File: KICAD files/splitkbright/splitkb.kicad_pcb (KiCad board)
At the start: 2 copper layers, 131.3 x 114.6 mm, 83 parts, among them SW31 SW_Push, SW32 SW_Push, SW37 SW_Push, SW38 SW_Push, SW39 SW_Push, SW40 SW_Push, SW41 SW_Push, SW42 SW_Push, SW43 SW_Push, SW44 SW_Push, SW45 SW_Push, SW46 SW_Push, SW47 SW_Push, SW48 SW_Push, SW49 SW_Push, SW50 SW_Push, SW51 SW_Push, SW52 SW_Push, SW53 SW_Push, SW54 SW_Push, SW55 SW_Push, SW56 SW_Push, SW57 SW_Push, SW58 SW_Push, SW59 SW_Push, SW60 SW_Push, SW61 SW_Push, SW62 SW_Push, SW63 SW_Push, SW64 SW_Push, SW65 SW_Push, SW66 SW_Push, SW67 SW_Push, SW68 SW_Push, SW69 SW_Push, SW70 SW_Push, SW71 SW_Push, SW72 SW_Push, SW73 SW_Push, SW74 SW_Push, U1 nice_nano

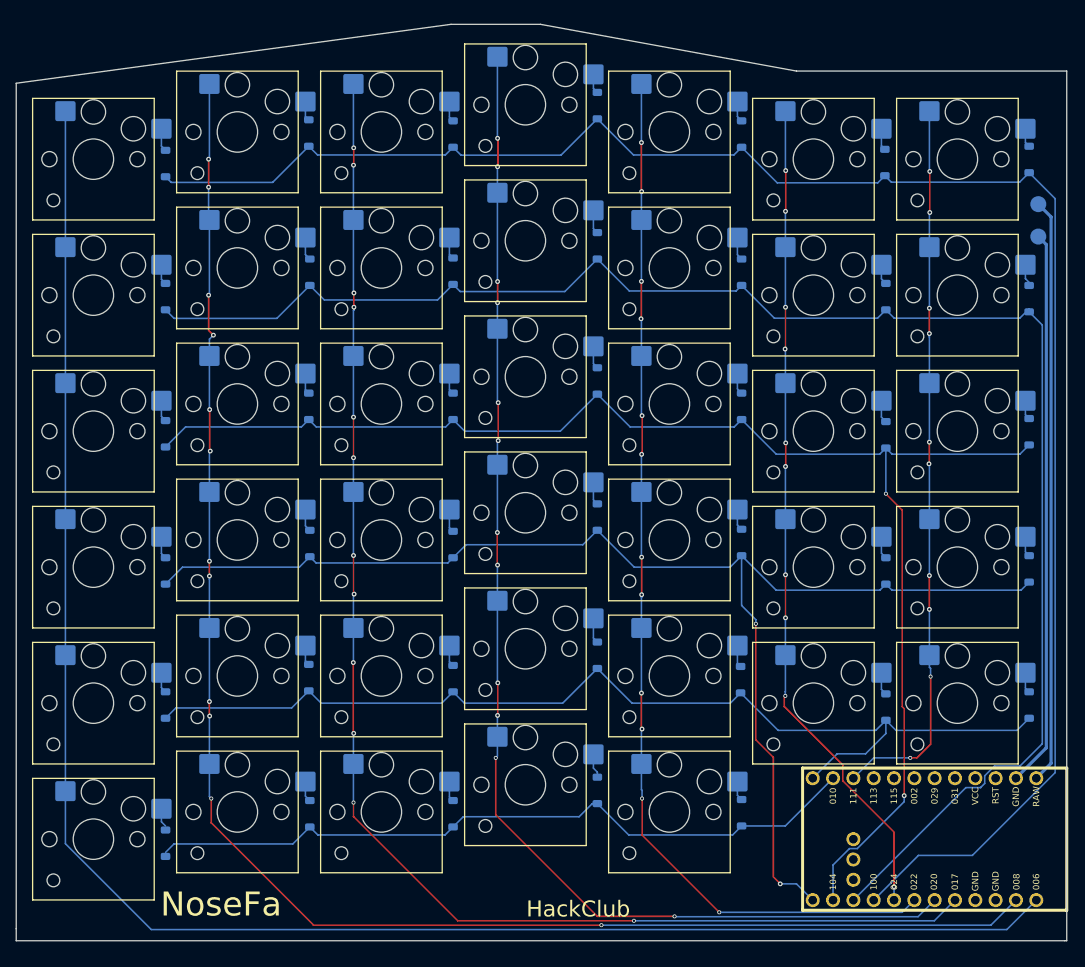
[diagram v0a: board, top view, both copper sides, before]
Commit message: Edited PCBs
- Added mounting holes to both pcbs and schematics
- Changed the shape and size of both PCBs
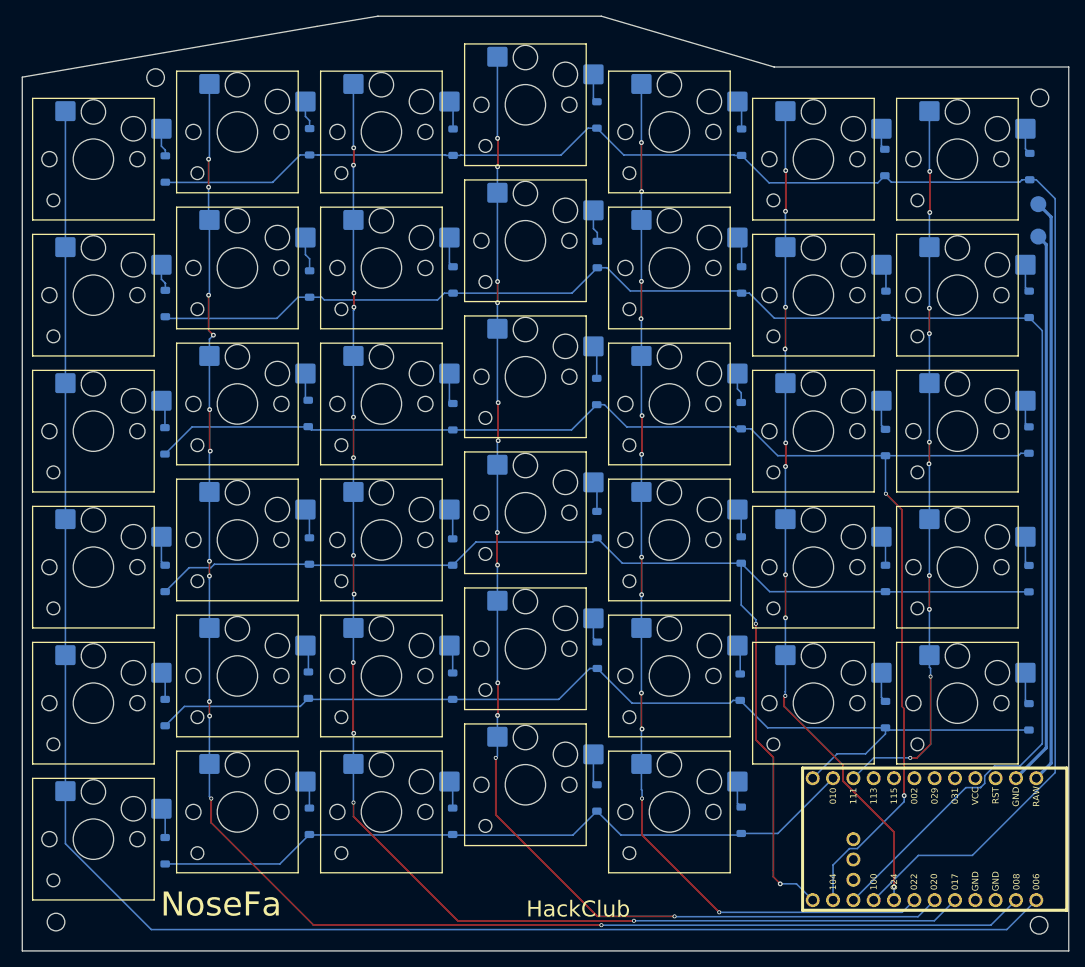
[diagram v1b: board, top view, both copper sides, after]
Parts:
- added REF**: MountingHole_2.2mm_M2, MountingHole:MountingHole_2.2mm_M2, F.Cu at (262.3, 43.3)
- added REF**: MountingHole_2.2mm_M2, MountingHole:MountingHole_2.2mm_M2, F.Cu at (139.3, 146.4)
- added REF**: MountingHole_2.2mm_M2, MountingHole:MountingHole_2.2mm_M2, F.Cu at (262.2, 146.8)
- added REF**: MountingHole_2.2mm_M2, MountingHole:MountingHole_2.2mm_M2, F.Cu at (151.8, 40.8)
- moved D58 1.47 mm to (171.0, 66.6)
- moved D73 1.47 mm to (260.9, 120.7)
- moved D47 1.32 mm to (206.9, 80.0)
- moved D53 1.30 mm to (188.9, 83.2)
- moved D72 1.22 mm to (260.9, 103.4)
- moved D42 1.17 mm to (225.0, 83.1)
- moved D45 1.17 mm to (206.9, 45.5)
- moved D57 1.10 mm to (171.0, 48.8)
- moved D46 1.09 mm to (207.0, 62.9)
- moved D52 1.09 mm to (189.0, 66.1)
- moved D71 1.04 mm to (260.9, 86.1)
- moved D40 1.02 mm to (225.0, 48.9)
- moved D51 1.02 mm to (189.0, 48.9)
- moved D37 0.97 mm to (243.0, 86.4)
- moved D32 0.97 mm to (243.1, 69.1)
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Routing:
- net row1: track 206.0 -> 199.9 mm
- net row4: track 132.0 -> 126.7 mm
- net row2: track 179.4 -> 174.4 mm
- net row0: track 224.2 -> 219.9 mm
- net row3: track 164.6 -> 160.7 mm
- net Net-(D73-A): track 2.58 -> 4.04 mm
- net Net-(D58-A): track 2.91 -> 4.37 mm
- net Net-(D68-A): track 2.36 -> 3.79 mm
- net Net-(D47-A): track 2.88 -> 4.17 mm
- net Net-(D53-A): track 2.64 -> 3.92 mm
- net Net-(D72-A): track 2.56 -> 3.77 mm
- net Net-(D45-A): track 2.46 -> 3.61 mm
- net Net-(D42-A): track 2.67 -> 3.81 mm
- net Net-(D57-A): track 2.46 -> 3.59 mm
- net Net-(D46-A): track 2.98 -> 4.08 mm
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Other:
- board size 131.3 x 114.6 mm -> 130.8 x 116.8 mm

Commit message: Edited PCB.
- Changed the footprint used for the dev board.
- Ran traces again for the dev board.
- Made a custom symbol and footprint for the devboard.
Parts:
- removed the REF** at (262.3, 43.3)
- removed the REF** at (139.3, 146.4)
- removed the REF** at (262.2, 146.8)
- removed the REF** at (151.8, 40.8)
- added D1: D, Diode_SMD:D_SOD-123, B.Cu at (52.8, 87.7)
- added D10: D, Diode_SMD:D_SOD-123, B.Cu at (106.9, 79.3)
- added D11: D, Diode_SMD:D_SOD-123, B.Cu at (124.8, 83.0)
- added D12: D, Diode_SMD:D_SOD-123, B.Cu at (52.8, 104.1)
- added D13: D, Diode_SMD:D_SOD-123, B.Cu at (71.0, 104.1)
- added D14: D, Diode_SMD:D_SOD-123, B.Cu at (88.9, 99.7)
- added D15: D, Diode_SMD:D_SOD-123, B.Cu at (106.9, 96.3)
- added D16: D, Diode_SMD:D_SOD-123, B.Cu at (124.9, 99.7)
- added D17: D, Diode_SMD:D_SOD-123, B.Cu at (52.9, 121.7)
- added D18: D, Diode_SMD:D_SOD-123, B.Cu at (70.7, 121.3)
- added D19: D, Diode_SMD:D_SOD-123, B.Cu at (88.9, 116.7)
- added D2: D, Diode_SMD:D_SOD-123, B.Cu at (52.8, 69.8)
- added D20: D, Diode_SMD:D_SOD-123, B.Cu at (106.9, 113.3)
- added D21: D, Diode_SMD:D_SOD-123, B.Cu at (124.9, 116.7)
- added D22: D, Diode_SMD:D_SOD-123, B.Cu at (52.8, 137.7)
- added D23: D, Diode_SMD:D_SOD-123, B.Cu at (70.9, 137.7)
- added D24: D, Diode_SMD:D_SOD-123, B.Cu at (88.9, 133.7)
- added D25: D, Diode_SMD:D_SOD-123, B.Cu at (106.9, 130.3)
- added D26: D, Diode_SMD:D_SOD-123, B.Cu at (124.8, 133.7)
- added D27: D, Diode_SMD:D_SOD-123, B.Cu at (142.8, 117.8)
- added D28: D, Diode_SMD:D_SOD-123, B.Cu at (142.9, 134.6)
- added D29: D, Diode_SMD:D_SOD-123, B.Cu at (142.9, 83.5)
- added D3: D, Diode_SMD:D_SOD-123, B.Cu at (70.8, 70.0)
- added D30: D, Diode_SMD:D_SOD-123, B.Cu at (142.9, 101.4)
- added D33: D, Diode_SMD:D_SOD-123, B.Cu at (88.9, 150.7)
- added D34: D, Diode_SMD:D_SOD-123, B.Cu at (106.9, 147.3)
- added D35: D, Diode_SMD:D_SOD-123, B.Cu at (124.9, 150.7)
- added D36: D, Diode_SMD:D_SOD-123, B.Cu at (142.9, 151.4)
- added D4: D, Diode_SMD:D_SOD-123, B.Cu at (88.9, 65.7)
- added D5: D, Diode_SMD:D_SOD-123, B.Cu at (106.9, 62.3)
- added D6: D, Diode_SMD:D_SOD-123, B.Cu at (124.9, 65.7)
- added D7: D, Diode_SMD:D_SOD-123, B.Cu at (143.0, 66.4)
- added D8: D, Diode_SMD:D_SOD-123, B.Cu at (70.7, 87.3)
- added D9: D, Diode_SMD:D_SOD-123, B.Cu at (88.9, 82.7)
- added H1: MountingHole, MountingHole:MountingHole_2.2mm_M2, F.Cu at (279.2, 56.8)
- added H10: MouseBite, Panelization.pretty-master:mouse-bite-5mm-slot, F.Cu at (149.5, 84.0)
- added H11: MouseBite, Panelization.pretty-master:mouse-bite-5mm-slot, F.Cu at (149.5, 147.2)
- added H12: MouseBite, Panelization.pretty-master:mouse-bite-5mm-slot, F.Cu at (149.4, 111.3)
- added H2: MountingHole, MountingHole:MountingHole_2.2mm_M2, F.Cu at (279.1, 160.2)
- added H3: MountingHole, MountingHole:MountingHole_2.2mm_M2, F.Cu at (156.2, 159.8)
- added H4: MountingHole, MountingHole:MountingHole_2.2mm_M2, F.Cu at (168.6, 54.3)
- added H9: MouseBite, Panelization.pretty-master:mouse-bite-5mm-slot, F.Cu at (149.5, 62.6)
- added REF**: MountingHole_2.2mm_M2, MountingHole:MountingHole_2.2mm_M2, F.Cu at (142.4, 163.1)
- added REF**: MountingHole_2.2mm_M2, MountingHole:MountingHole_2.2mm_M2, F.Cu at (143.9, 57.0)
- added REF**: MountingHole_2.2mm_M2, MountingHole:MountingHole_2.2mm_M2, F.Cu at (53.0, 59.0)
- added REF**: MountingHole_2.2mm_M2, MountingHole:MountingHole_2.2mm_M2, F.Cu at (34.7, 168.7)
- added SW1: SW_Push, PCM_Switch_Keyboard_Hotswap_Kailh:SW_Hotswap_Kailh_Choc_V1V2, F.Cu at (43.8, 69.1)
- added SW10: SW_Push, PCM_Switch_Keyboard_Hotswap_Kailh:SW_Hotswap_Kailh_Choc_V1V2, F.Cu at (97.8, 78.4)
- added SW11: SW_Push, PCM_Switch_Keyboard_Hotswap_Kailh:SW_Hotswap_Kailh_Choc_V1V2, F.Cu at (115.8, 81.8)
- added SW12: SW_Push, PCM_Switch_Keyboard_Hotswap_Kailh:SW_Hotswap_Kailh_Choc_V1V2, F.Cu at (133.8, 82.7)
- added SW13: SW_Push, PCM_Switch_Keyboard_Hotswap_Kailh:SW_Hotswap_Kailh_Choc_V1V2, F.Cu at (43.8, 103.1)
- added SW14: SW_Push, PCM_Switch_Keyboard_Hotswap_Kailh:SW_Hotswap_Kailh_Choc_V1V2, F.Cu at (61.8, 103.1)
- added SW15: SW_Push, PCM_Switch_Keyboard_Hotswap_Kailh:SW_Hotswap_Kailh_Choc_V1V2, F.Cu at (79.8, 98.8)
- added SW16: SW_Push, PCM_Switch_Keyboard_Hotswap_Kailh:SW_Hotswap_Kailh_Choc_V1V2, F.Cu at (97.8, 95.4)
- added SW17: SW_Push, PCM_Switch_Keyboard_Hotswap_Kailh:SW_Hotswap_Kailh_Choc_V1V2, F.Cu at (115.8, 98.8)
- added SW18: SW_Push, PCM_Switch_Keyboard_Hotswap_Kailh:SW_Hotswap_Kailh_Choc_V1V2, F.Cu at (133.8, 99.7)
- added SW19: SW_Push, PCM_Switch_Keyboard_Hotswap_Kailh:SW_Hotswap_Kailh_Choc_V1V2, F.Cu at (43.8, 120.1)
- added SW2: SW_Push, PCM_Switch_Keyboard_Hotswap_Kailh:SW_Hotswap_Kailh_Choc_V1V2, F.Cu at (61.8, 69.1)
- added SW20: SW_Push, PCM_Switch_Keyboard_Hotswap_Kailh:SW_Hotswap_Kailh_Choc_V1V2, F.Cu at (61.8, 120.1)
- added SW21: SW_Push, PCM_Switch_Keyboard_Hotswap_Kailh:SW_Hotswap_Kailh_Choc_V1V2, F.Cu at (79.8, 115.8)
- added SW22: SW_Push, PCM_Switch_Keyboard_Hotswap_Kailh:SW_Hotswap_Kailh_Choc_V1V2, F.Cu at (97.8, 112.4)
- added SW23: SW_Push, PCM_Switch_Keyboard_Hotswap_Kailh:SW_Hotswap_Kailh_Choc_V1V2, F.Cu at (115.8, 115.8)
- added SW24: SW_Push, PCM_Switch_Keyboard_Hotswap_Kailh:SW_Hotswap_Kailh_Choc_V1V2, F.Cu at (133.8, 116.7)
- added SW25: SW_Push, PCM_Switch_Keyboard_Hotswap_Kailh:SW_Hotswap_Kailh_Choc_V1V2, F.Cu at (43.8, 137.1)
- added SW26: SW_Push, PCM_Switch_Keyboard_Hotswap_Kailh:SW_Hotswap_Kailh_Choc_V1V2, F.Cu at (61.8, 137.1)
- added SW27: SW_Push, PCM_Switch_Keyboard_Hotswap_Kailh:SW_Hotswap_Kailh_Choc_V1V2, F.Cu at (79.8, 132.8)
- added SW28: SW_Push, PCM_Switch_Keyboard_Hotswap_Kailh:SW_Hotswap_Kailh_Choc_V1V2, F.Cu at (97.8, 129.4)
- added SW29: SW_Push, PCM_Switch_Keyboard_Hotswap_Kailh:SW_Hotswap_Kailh_Choc_V1V2, F.Cu at (115.8, 132.8)
- added SW3: SW_Push, PCM_Switch_Keyboard_Hotswap_Kailh:SW_Hotswap_Kailh_Choc_V1V2, F.Cu at (79.8, 64.8)
- added SW30: SW_Push, PCM_Switch_Keyboard_Hotswap_Kailh:SW_Hotswap_Kailh_Choc_V1V2, F.Cu at (133.8, 133.7)
- added SW33: SW_Push, PCM_Switch_Keyboard_Hotswap_Kailh:SW_Hotswap_Kailh_Choc_V1V2, F.Cu at (79.8, 149.8)
- added SW34: SW_Push, PCM_Switch_Keyboard_Hotswap_Kailh:SW_Hotswap_Kailh_Choc_V1V2, F.Cu at (97.8, 146.4)
- added SW35: SW_Push, PCM_Switch_Keyboard_Hotswap_Kailh:SW_Hotswap_Kailh_Choc_V1V2, F.Cu at (115.8, 149.8)
- added SW36: SW_Push, PCM_Switch_Keyboard_Hotswap_Kailh:SW_Hotswap_Kailh_Choc_V1V2, F.Cu at (133.8, 150.7)
- added SW4: SW_Push, PCM_Switch_Keyboard_Hotswap_Kailh:SW_Hotswap_Kailh_Choc_V1V2, F.Cu at (97.8, 61.4)
- added SW5: SW_Push, PCM_Switch_Keyboard_Hotswap_Kailh:SW_Hotswap_Kailh_Choc_V1V2, F.Cu at (115.8, 64.8)
- added SW6: SW_Push, PCM_Switch_Keyboard_Hotswap_Kailh:SW_Hotswap_Kailh_Choc_V1V2, F.Cu at (133.8, 65.7)
- added SW7: SW_Push, PCM_Switch_Keyboard_Hotswap_Kailh:SW_Hotswap_Kailh_Choc_V1V2, F.Cu at (43.8, 86.1)
- added SW8: SW_Push, PCM_Switch_Keyboard_Hotswap_Kailh:SW_Hotswap_Kailh_Choc_V1V2, F.Cu at (61.8, 86.1)
- added SW9: SW_Push, PCM_Switch_Keyboard_Hotswap_Kailh:SW_Hotswap_Kailh_Choc_V1V2, F.Cu at (79.8, 81.8)
- added TP1: Bat, TestPoint:TestPoint_Pad_D2.0mm, B.Cu at (143.4, 75.2)
- added TP2: Gnd, TestPoint:TestPoint_Pad_D2.0mm, B.Cu at (143.4, 70.7)
- added U2: NRF52840, nice-nano-kicad-master:NRF52840, B.Cu at (50.2, 157.5)
- U1: value nice_nano -> NRF52840; footprint nice-nano-kicad-master:nice_nano -> nice-nano-kicad-master:NRF52840
- moved D39 21.6 mm to (259.9, 133.9)
- moved D37 21.6 mm to (259.9, 99.9)
- moved D38 21.6 mm to (259.9, 116.9)
- moved D32 21.6 mm to (259.9, 82.6)
- moved D41 21.6 mm to (241.9, 79.6)
- moved D44 21.6 mm to (241.7, 130.5)
- moved D50 21.6 mm to (223.8, 144.3)
- moved D52 21.6 mm to (205.8, 79.6)
- moved D53 21.6 mm to (205.8, 96.7)
- moved D54 21.6 mm to (205.8, 113.6)
- moved D55 21.6 mm to (205.8, 130.3)
- moved D64 21.6 mm to (169.8, 82.5)
- moved D65 21.6 mm to (169.8, 99.7)
- moved D70 21.6 mm to (277.8, 82.6)
- moved D74 21.6 mm to (241.8, 147.1)
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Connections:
- D31 pad 1: row0 -> Rrow0
- D32 pad 1: row1 -> Rrow1
- D37 pad 1: row2 -> Rrow2
- D38 pad 1: row3 -> Rrow3
- D39 pad 1: row4 -> Rrow4
- D40 pad 1: row0 -> Rrow0
- D41 pad 1: row1 -> Rrow1
- D42 pad 1: row2 -> Rrow2
- D43 pad 1: row3 -> Rrow3
- D44 pad 1: row4 -> Rrow4
- D45 pad 1: row0 -> Rrow0
- D46 pad 1: row1 -> Rrow1
- D47 pad 1: row2 -> Rrow2
- D48 pad 1: row3 -> Rrow3
- D49 pad 1: row4 -> Rrow4
- D50 pad 1: row5 -> Rrow5
- D51 pad 1: row0 -> Rrow0
- D52 pad 1: row1 -> Rrow1
- D53 pad 1: row2 -> Rrow2
- D54 pad 1: row3 -> Rrow3
- D55 pad 1: row4 -> Rrow4
- D56 pad 1: row5 -> Rrow5
- D57 pad 1: row0 -> Rrow0
- D58 pad 1: row1 -> Rrow1
- D59 pad 1: row2 -> Rrow2
- D60 pad 1: row3 -> Rrow3
- D61 pad 1: row4 -> Rrow4
- D62 pad 1: row5 -> Rrow5
- D63 pad 1: row0 -> Rrow0
- D64 pad 1: row1 -> Rrow1
- D65 pad 1: row2 -> Rrow2
- D66 pad 1: row3 -> Rrow3
- D67 pad 1: row4 -> Rrow4
- D68 pad 1: row5 -> Rrow5
- D69 pad 1: row0 -> Rrow0
- D70 pad 1: row1 -> Rrow1
- D71 pad 1: row2 -> Rrow2
- D72 pad 1: row3 -> Rrow3
- D73 pad 1: row4 -> Rrow4
- D74 pad 1: row5 -> Rrow5
- SW31 pad 1: col5 -> Rcol5
- SW32 pad 1: col5 -> Rcol5
- SW37 pad 1: col5 -> Rcol5
- SW38 pad 1: col5 -> Rcol5
- SW39 pad 1: col5 -> Rcol5
- SW40 pad 1: col4 -> Rcol4
- SW41 pad 1: col4 -> Rcol4
- SW42 pad 1: col4 -> Rcol4
- SW43 pad 1: col4 -> Rcol4
- SW44 pad 1: col4 -> Rcol4
- SW45 pad 1: col3 -> Rcol3
- SW46 pad 1: col3 -> Rcol3
- SW47 pad 1: col3 -> Rcol3
- SW48 pad 1: col3 -> Rcol3
- SW49 pad 1: col3 -> Rcol3
- SW50 pad 1: col3 -> Rcol3
- SW51 pad 1: col2 -> Rcol2
- SW52 pad 1: col2 -> Rcol2
- SW53 pad 1: col2 -> Rcol2
- SW54 pad 1: col2 -> Rcol2
- SW55 pad 1: col2 -> Rcol2
- SW56 pad 1: col2 -> Rcol2
- SW57 pad 1: col1 -> Rcol1
- SW58 pad 1: col1 -> Rcol1
- SW59 pad 1: col1 -> Rcol1
- SW60 pad 1: col1 -> Rcol1
- SW61 pad 1: col1 -> Rcol1
- SW62 pad 1: col1 -> Rcol1
- SW63 pad 1: col0 -> Rcol0
- SW64 pad 1: col0 -> Rcol0
- SW65 pad 1: col0 -> Rcol0
- SW66 pad 1: col0 -> Rcol0
- SW67 pad 1: col0 -> Rcol0
- SW68 pad 1: col0 -> Rcol0
- SW69 pad 1: col6 -> Rcol6
- SW70 pad 1: col6 -> Rcol6
- SW71 pad 1: col6 -> Rcol6
- SW72 pad 1: col6 -> Rcol6
- SW73 pad 1: col6 -> Rcol6
- SW74 pad 1: col4 -> Rcol4
- TP1 pad 1: bat -> Rbat
- TP2 pad 1: GND -> RGND
- U1 pad 1: col0 -> unconnected-(U1-GND-Pad1)
- U1 pad 10: row1 -> Rrow0
- U1 pad 11: row2 -> Rrow1
- U1 pad 12: row3 -> Rrow2
- U1 pad 13: row4 -> Rrow3
- U1 pad 14: row5 -> Rrow4
- U1 pad 15: col6 -> Rrow5
- U1 pad 16: unconnected-(U1-P1.13-Pad16) -> Rcol6
- U1 pad 2: col1 -> Rcol0
- U1 pad 23: GND -> unconnected-(U1-RESET-Pad23)
- U1 pad 24: bat -> RGND
- U1 pad 3: unconnected-(U1-GND-Pad3) -> Rcol1
- U1 pad 5: col2 -> unconnected-(U1-GND-Pad5)
- U1 pad 6: col3 -> Rcol2
- U1 pad 7: col4 -> Rcol3
- U1 pad 8: col5 -> Rcol4
- U1 pad 9: row0 -> Rcol5
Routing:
- net Rrow0: track 0.00 -> 231.8 mm, vias 0 -> 1
- net Rcol0: track 0.00 -> 218.5 mm
- net Rrow1: track 0.00 -> 201.0 mm
- net Rcol1: track 0.00 -> 200.0 mm, vias 0 -> 12
- net Rrow2: track 0.00 -> 173.5 mm, vias 0 -> 2
- net Rcol2: track 0.00 -> 173.1 mm, vias 0 -> 12
- net Rrow3: track 0.00 -> 159.5 mm, vias 0 -> 2
- net Rcol3: track 0.00 -> 155.7 mm, vias 0 -> 12
- net Rcol4: track 0.00 -> 132.7 mm, vias 0 -> 12
- net col0: track 218.9 -> 89.1 mm
- net Rrow4: track 0.00 -> 127.2 mm
- net GND: track 69.7 -> 196.7 mm
- net bat: track 73.2 -> 198.7 mm, vias 0 -> 2
- net Rcol5: track 0.00 -> 103.7 mm, vias 0 -> 9
- net col1: track 200.3 -> 98.6 mm, vias 12 -> 10
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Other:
- board size 130.8 x 116.8 mm -> 250.6 x 125.7 mm
